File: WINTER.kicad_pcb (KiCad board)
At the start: 6 copper layers, 52 x 34 mm, 107 parts, among them J1 Amphenol ICC 10118193-0001LF, J2 TF-102-15, J3 Screw_Terminal_01x12, J4 Screw_Terminal_01x02, J5 Conn_01x05, J6 Conn_01x04, Q1 SI7232DN-T1-GE3, Q2 SI7232DN-T1-GE3, Q3 SI7232DN-T1-GE3, SW1 A6S-2104-H, U1 LM2940LD-5.0/NOPB, U10 SX1262IMLTRT, U11 MAX-M10S-00B, U12 LM1117LD-3.3/NOPB, U13 74LVC1G04, U15 TPS7A20xxxDQN, U2 DRV8210DRLR, U3 MMC5983MA, U4 ICM-42688-P, U5 SKY66105, U6 STM32H725RGV6, U7 MS5607-02BA, U8 ADXL375, U9 SN74LVC2T45DC, Y1 ECS-2520MV-240-BN, Y2 ATX-11-F-32.000MHZ-F05-T

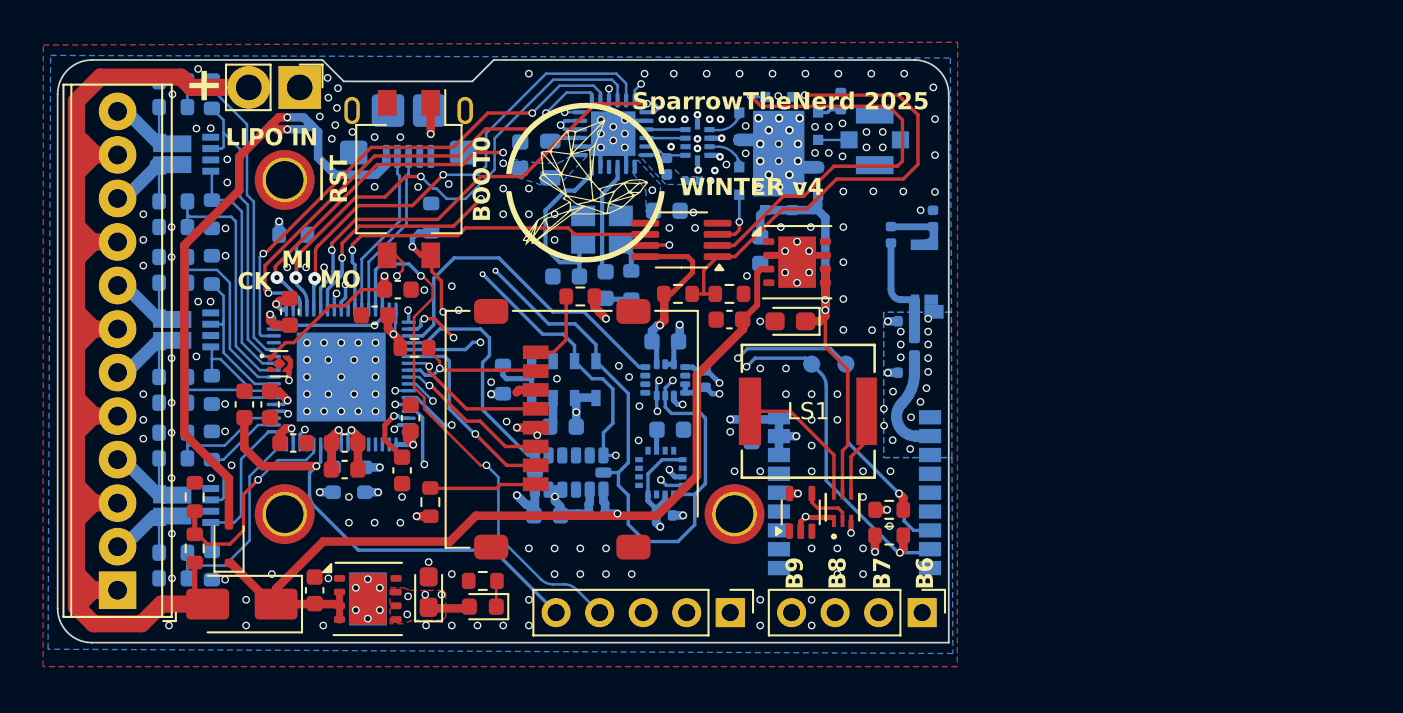
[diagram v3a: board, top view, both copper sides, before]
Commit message: Started new layout and updated power circuitry
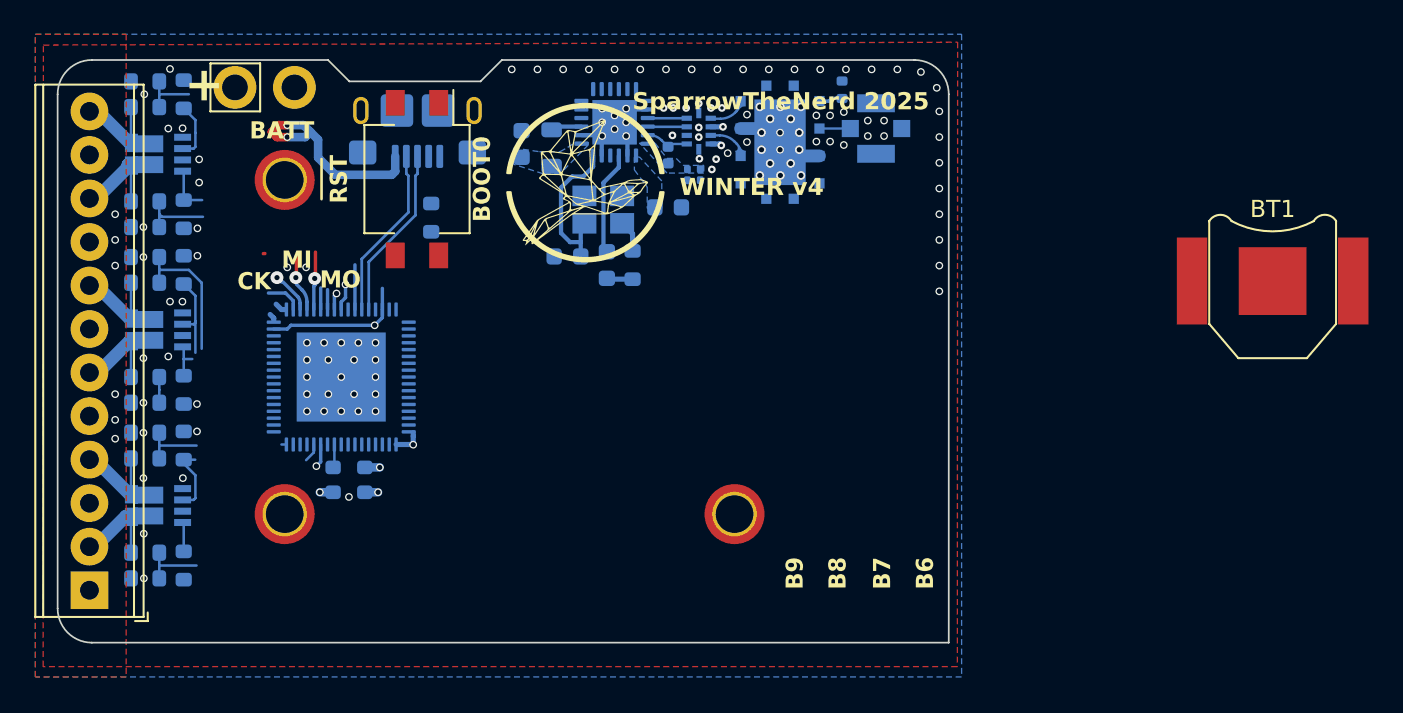
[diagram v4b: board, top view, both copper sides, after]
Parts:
- removed AE2: GGBLA.01.A, WINTERfootprints:GGBLA.01.A
- removed C1, C3: 2.2uF, Capacitor_SMD:C_0603_1608Metric
- removed C10: 4.7uF, Capacitor_SMD:C_0603_1608Metric
- removed C11: 470nF, Capacitor_SMD:C_0603_1608Metric
- removed C12: 22uF, Capacitor_SMD:C_0603_1608Metric
- removed C13, C14: 47uF tant, Capacitor_Tantalum_SMD:CP_EIA-2012-15_AVX-P
- removed C15, C19: 1uF, Capacitor_SMD:C_0402_1005Metric
- removed C16, C2, C20, C21, C26, C29, C4, C5, C6, C7, C8, C9: 100nF, Capacitor_SMD:C_0603_1608Metric
- removed C17: 10uF, Capacitor_SMD:C_0603_1608Metric
- removed C18: 2.2uF, Capacitor_SMD:C_0402_1005Metric
- removed C30: 0.8pF, Capacitor_SMD:C_0402_1005Metric
- removed C31: 2.7pF, Capacitor_SMD:C_0402_1005Metric
- removed C32: 0.5pF, Capacitor_SMD:C_0402_1005Metric
- removed C33: 22pF, Capacitor_SMD:C_0402_1005Metric
- removed C34: DNP, Capacitor_SMD:C_0402_1005Metric
- removed D1: RSX501L-20TE25, Diode_SMD:D_SMA
- removed D2: PMEG3020EJ, Diode_SMD:D_SOD-323F
- removed D3: LED_RD, LED_SMD:LED_0603_1608Metric
- removed J2: TF-102-15, Connector_Card:microSD_HC_Molex_47219-2001
- removed J5: Conn_01x05, Connector_PinHeader_2.54mm:PinHeader_1x05_P2.54mm_Vertical
- removed J6: Conn_01x04, Connector_PinHeader_2.54mm:PinHeader_1x04_P2.54mm_Vertical
- removed LS1: AST0760MCTRQ, WINTERfootprints:AST0760_MAL
- removed R22, R23, R5, R6: 10k, Resistor_SMD:R_0603_1608Metric
- removed R24, R30: 27k, Resistor_SMD:R_0603_1608Metric
- removed R28, R29, R3, R4: 4.7k, Resistor_SMD:R_0603_1608Metric
- removed R31: 100k, Resistor_SMD:R_0603_1608Metric
- removed R7: 470, Resistor_SMD:R_0603_1608Metric
- removed TP1, TP2: TestPoint, TestPoint:TestPoint_Pad_D1.0mm
- removed U1: LM2940LD-5.0/NOPB, Package_SON:WSON-8-1EP_4x4mm_P0.8mm_EP2.2x3mm
- removed U11: MAX-M10S-00B, WINTERfootprints:MAX-M10S-00B
- removed U12: LM1117LD-3.3/NOPB, Package_SON:WSON-8-1EP_4x4mm_P0.8mm_EP2.2x3mm
- removed U13: 74LVC1G04, Package_TO_SOT_SMD:Texas_R-PDSO-G5_DCK-5
- removed U15: TPS7A20xxxDQN, Package_SON:Texas_X2SON-4_1x1mm_P0.65mm
- removed U2: DRV8210DRLR, WINTERfootprints:SOT_210DRLR_TEX
- removed U3: MMC5983MA, WINTERfootprints:MMC5983MA_MEM
- removed U4: ICM-42688-P, WINTERfootprints:PQFN50P300X250X97-14N
- removed U7: MS5607-02BA, Package_LGA:LGA-8_3x5mm_P1.25mm
- removed U8: ADXL375, Package_LGA:LGA-14_3x5mm_P0.8mm_LayoutBorder1x6y
- removed U9: SN74LVC2T45DC, Package_SO:MSOP-8_3x3mm_P0.65mm
- added BT1: 2998TR, Battery:BatteryHolder_Keystone_2998_1x6.8mm, F.Cu at (208.9, 96.9)
- moved J3 1.64 mm to (139.9, 114.9)
- moved Q1 1.64 mm to (143.9, 110.0)
- moved Q2 1.64 mm to (143.9, 99.8)
- moved Q3 1.64 mm to (143.9, 89.5)
- moved R10 1.64 mm to (143.1, 104.0)
- moved R11 1.64 mm to (143.1, 95.5)
- moved R14 1.64 mm to (145.4, 113.5)
- moved R15 1.64 mm to (145.4, 106.5)
- moved R16 1.64 mm to (145.4, 103.2)
- moved R17 1.64 mm to (145.4, 96.2)
- moved R18 1.64 mm to (145.4, 93.0)
- moved R19 1.64 mm to (145.4, 86.0)
- moved R20 1.64 mm to (143.1, 114.2)
- moved R32 1.64 mm to (143.1, 107.2)
- moved R33 1.64 mm to (143.1, 93.8)
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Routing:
- net LIPO+: track 79.8 -> 0.00 mm, vias 0 -> 1
- net SCL: track 73.0 -> 1.57 mm, vias 5 -> 1
- net +3V3: track 67.1 -> 3.98 mm, vias 39 -> 3
- net SDA: track 62.1 -> 0.99 mm, vias 8 -> 1
- net Net-(D1-K): track 51.1 -> 0.00 mm
- net SWD-NRST: track 48.0 -> 1.37 mm, vias 2 -> 1
- net SWCLK: track 40.6 -> 0.00 mm, vias 1 -> 0
- net SERVO4: track 37.0 -> 0.00 mm, vias 1 -> 0
- net SERVO3: track 35.0 -> 0.00 mm, vias 1 -> 0
- net BUZZ: track 33.8 -> 0.00 mm, vias 3 -> 0
- net SERVO2: track 33.2 -> 0.00 mm, vias 1 -> 0
- net SCK_LoRa: track 33.8 -> 2.47 mm, vias 3 -> 1
- net SWDIO: track 31.3 -> 0.00 mm, vias 2 -> 0
- net LoRa_BUSY: track 29.7 -> 0.10 mm, vias 2 -> 0
- net SERVO1: track 29.4 -> 0.00 mm, vias 1 -> 0
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- added copper zone on F.Cu, net LIPO+
- added copper zone on In2.Cu, net LIPO+
- added copper zone on In3.Cu, net LIPO+
- removed copper zone on F.Cu, net +3V3
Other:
- outline, holes or cut-outs redrawn
- board text added: "BATT"
- board text removed: "LIPO IN"

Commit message: updated power delivery and component choices. v4 now ready
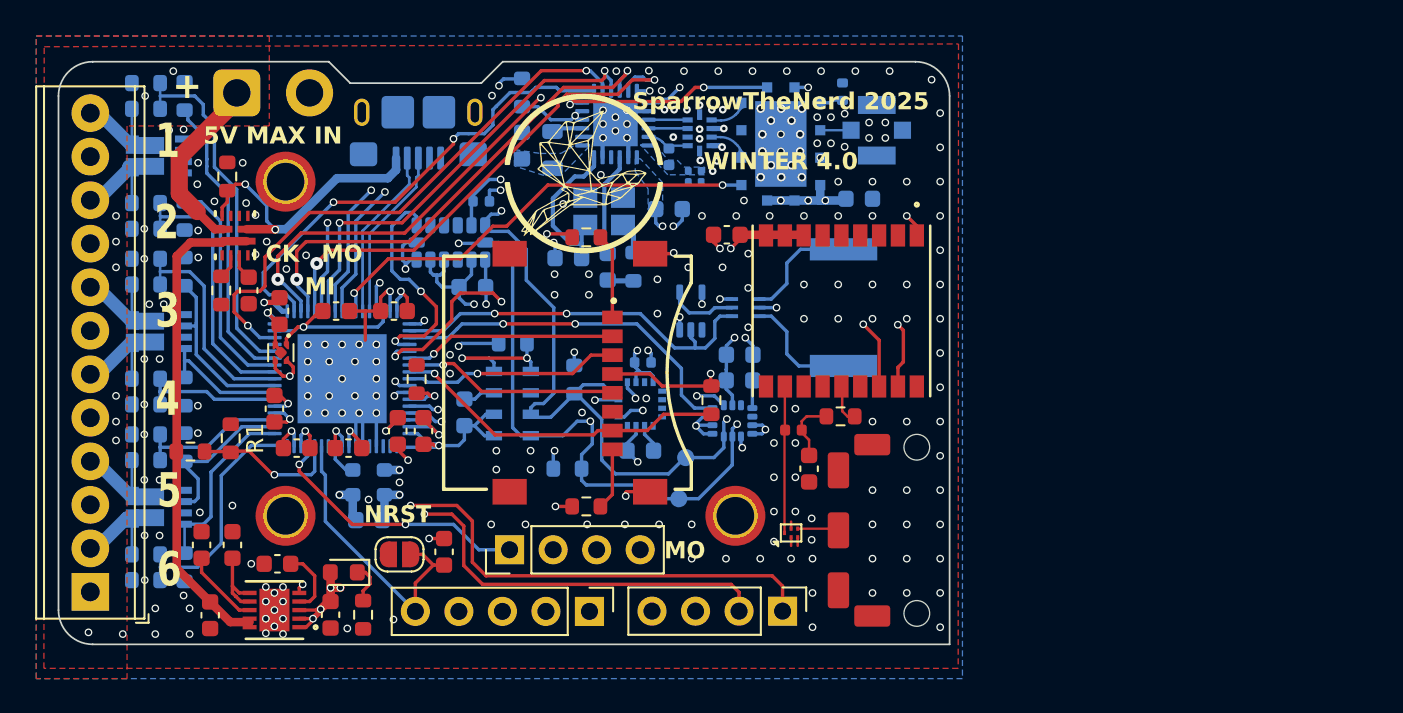
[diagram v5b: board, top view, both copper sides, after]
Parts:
- removed BT1: 2998TR, Battery:BatteryHolder_Keystone_2998_1x6.8mm
- removed SW1: A6S-2104-H, Button_Switch_SMD:SW_DIP_SPSTx02_Slide_Omron_A6S-210x_W8.9mm_P2.54mm
- added AE2: AP.10H.01, WINTERfootprints:AP.10H.01, F.Cu at (183.6, 111.4)
- added C1: 2.2uF, Capacitor_SMD:C_0603_1608Metric, F.Cu at (154.2, 98.7)
- added C10: 4.7uF, Capacitor_SMD:C_0603_1608Metric, B.Cu at (156.2, 110.8)
- added C11: 22uF, Capacitor_SMD:C_0603_1608Metric, F.Cu at (153.9, 116.4)
- added C12: 22uF, Capacitor_SMD:C_0603_1608Metric, F.Cu at (146.9, 116.4)
- added C13: 10nF, Capacitor_SMD:C_0603_1608Metric, F.Cu at (181.8, 107.8)
- added C14: 100nF, Capacitor_SMD:C_0603_1608Metric, F.Cu at (149.2, 97.5)
- added C15: 1uF, Capacitor_SMD:C_0402_1005Metric, B.Cu at (172.2, 101.7)
- added C16: 100nF, Capacitor_SMD:C_0603_1608Metric, B.Cu at (177.8, 102.7)
- added C17: 10nF, Capacitor_SMD:C_0603_1608Metric, B.Cu at (172.0, 106.8)
- added C18: 2.2uF, Capacitor_SMD:C_0603_1608Metric, B.Cu at (177.8, 101.2)
- added C19: 1uF, Capacitor_SMD:C_0402_1005Metric, B.Cu at (162.7, 92.2)
- added C2: 100nF, Capacitor_SMD:C_0603_1608Metric, F.Cu at (160.6, 112.7)
- added C20: 100nF, Capacitor_SMD:C_0603_1608Metric, B.Cu at (162.2, 97.2)
- added C21: 100nF, Capacitor_SMD:C_0603_1608Metric, B.Cu at (161.7, 104.6)
- added C26: 100nF, Capacitor_SMD:C_0603_1608Metric, B.Cu at (184.8, 92.1)
- added C29: 100nF, Capacitor_SMD:C_0603_1608Metric, F.Cu at (177.1, 94.2)
- added C3: 2.2uF, Capacitor_SMD:C_0603_1608Metric, F.Cu at (157.8, 105.7)
- added C30: 22uF, Capacitor_SMD:C_0603_1608Metric, F.Cu at (146.4, 112.3)
- added C31: 22uF, Capacitor_SMD:C_0603_1608Metric, F.Cu at (148.2, 112.3)
- added C32: 22uF, Capacitor_SMD:C_0603_1608Metric, F.Cu at (150.8, 113.4)
- added C4: 100nF, Capacitor_SMD:C_0603_1608Metric, F.Cu at (150.7, 104.3)
- added C5: 100nF, Capacitor_SMD:C_0603_1608Metric, F.Cu at (155.0, 106.7)
- added C6: 100nF, Capacitor_SMD:C_0603_1608Metric, F.Cu at (151.9, 106.7)
- added C7: 100nF, Capacitor_SMD:C_0603_1608Metric, F.Cu at (150.9, 98.7)
- added C8: 100nF, Capacitor_SMD:C_0603_1608Metric, F.Cu at (159.3, 105.7)
- added C9: 100nF, Capacitor_SMD:C_0603_1608Metric, F.Cu at (157.6, 98.7)
- added D3: LED_RD, LED_SMD:LED_0603_1608Metric, F.Cu at (154.7, 113.9)
- added FL2: B39162B8813P810, Filter:Filter_1109-5_1.1x0.9mm, F.Cu at (180.8, 111.6)
- added J2: TF-102-15, WINTERfootprints:microSD_GCT_MEM2067-02-180-00, F.Cu at (167.8, 102.2)
- added J5: Conn_01x05, Connector_PinHeader_2.54mm:PinHeader_1x05_P2.54mm_Vertical, F.Cu at (169.0, 116.2)
- added J6: Conn_01x04, Connector_PinHeader_2.54mm:PinHeader_1x04_P2.54mm_Vertical, F.Cu at (180.3, 116.2)
- added J7: Conn_01x04, Connector_PinHeader_2.54mm:PinHeader_1x04_P2.54mm_Vertical, F.Cu at (164.4, 112.6)
- added JP1: SolderJumper_2_Open, Jumper:SolderJumper-2_P1.3mm_Open_RoundedPad1.0x1.5mm, F.Cu at (157.9, 112.8)
- added L3: 27nH, Inductor_SMD:L_0402_1005Metric, F.Cu at (180.9, 105.6)
- added LS1: AST0760MCTRQ, WINTERfootprints:AST0760_MAL, B.Cu at (183.9, 98.5)
- added R1: 27k, Resistor_SMD:R_0603_1608Metric, F.Cu at (148.1, 106.1)
- added R12: 27k, Resistor_SMD:R_0603_1608Metric, F.Cu at (147.9, 90.8)
- added R13: 27k, Resistor_SMD:R_0603_1608Metric, F.Cu at (147.6, 97.5)
- added R21: 10, 0.25W, Resistor_SMD:R_0603_1608Metric, F.Cu at (183.7, 104.8)
- added R22: 10k, Resistor_SMD:R_0603_1608Metric, B.Cu at (164.6, 100.5)
- added R28: 4.7k, Resistor_SMD:R_0603_1608Metric, F.Cu at (168.8, 110.0)
- added R29: 4.7k, Resistor_SMD:R_0603_1608Metric, F.Cu at (168.8, 94.3)
- added R3: 4.7k, Resistor_SMD:R_0603_1608Metric, F.Cu at (176.2, 103.8)
- added R30: 27k, Resistor_SMD:R_0603_1608Metric, F.Cu at (145.8, 106.8)
- added R4: 4.7k, Resistor_SMD:R_0603_1608Metric, B.Cu at (165.1, 85.9)
- added R5: 4.7k, Resistor_SMD:R_0603_1608Metric, B.Cu at (168.2, 102.7)
- added R6: 4.7k, Resistor_SMD:R_0603_1608Metric, B.Cu at (167.8, 107.8)
- added R7: 470, Resistor_SMD:R_0603_1608Metric, F.Cu at (155.8, 116.4)
- added TP1: TestPoint, TestPoint:TestPoint_Pad_D1.0mm, B.Cu at (174.7, 107.2)
- added TP2: TestPoint, TestPoint:TestPoint_Pad_D1.0mm, B.Cu at (174.2, 109.6)
- added U1: ADP7158ACPZ-3.3-R7, WINTERfootprints:CP-10-9_ADI, F.Cu at (150.7, 116.1)
- added U11: MAX-M10S-00B, WINTERfootprints:MAX-M10S-00B, F.Cu at (183.7, 98.6)
- added U12: TPS2121RUXR, WINTERfootprints:RUX0012A, F.Cu at (148.3, 94.2)
- added U13: 74LVC1G04, Package_TO_SOT_SMD:Texas_R-PDSO-G5_DCK-5, B.Cu at (174.9, 98.7)
- added U15: TPS7A20135PDQNR, Package_SON:Texas_X2SON-4_1x1mm_P0.65mm, F.Cu at (151.0, 101.1)
- added U2: DRV8210DRLR, WINTERfootprints:SOT_210DRLR_TEX, B.Cu at (178.2, 98.5)
- added U3: MMC5983MA, WINTERfootprints:MMC5983MA_MEM, B.Cu at (172.0, 104.1)
- added U4: ICM-42688-P, WINTERfootprints:PQFN50P300X250X97-14N, B.Cu at (177.4, 105.1)
- added U7: MS5607-02BA, Package_LGA:LGA-8_3x5mm_P1.25mm, B.Cu at (164.5, 104.0)
- added U8: ADXL375, Package_LGA:LGA-14_3x5mm_P0.8mm_LayoutBorder1x6y, B.Cu at (160.9, 94.7)
- J4: footprint Connector_PinHeader_2.54mm:PinHeader_1x02_P2.54mm_Vertical -> Connector_Wire:SolderWire-0.75sqmm_1x02_P7mm_D1.25mm_OD3.5mm
- R10, R11, R20, R33, R34, R9: value 100k -> 27k
- R2: moved to F.Cu
- moved R2 9.46 mm to (158.9, 102.6)
- moved J4 2.88 mm to (148.5, 85.9), turned to 0 degrees
- moved Y1 1.16 mm to (156.1, 108.6)
- moved R25 0.12 mm to (183.8, 85.8)
- moved C23 0.11 mm to (173.7, 92.7)
- moved C24 0.11 mm to (175.6, 90.8)
- moved J3 0.11 mm to (139.9, 115.0)
- moved C25 0.11 mm to (174.8, 90.8)
- moved C28 0.11 mm to (167.8, 95.6)
- moved FL1 0.11 mm to (175.5, 88.2)
- moved H1 0.11 mm to (151.3, 91.1)
- moved H2 0.11 mm to (177.6, 110.6)
- moved H3 0.11 mm to (151.3, 110.6)
- moved J1 0.11 mm to (159.1, 87.0)
- moved L2 0.11 mm to (173.7, 89.7)
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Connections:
- net /Microcontroller/SWD-BOOT0 renamed Net-(U6-BOOT0)
- J1 pad 1: Net-(D2-A) -> /Power/VBUS
- J4 pad 1: GNDREF -> LIPO+
- J4 pad 2: LIPO+ -> GNDREF
- U5 pad 1: /LoRa Radio/PA-EN-2v5 -> LoRa_PA-EN
- U5 pad 10: +5V -> +3V3
- U5 pad 11: +5V -> +3V3
- U5 pad 12: +5V -> +3V3
- U5 pad 5: /LoRa Radio/DIO2-2v5 -> /LoRa Radio/DIO2
- U5 pad 6: +2V5 -> +3V3
- U6 pad 12: SWD-NRST -> NRST
- U6 pad 14: unconnected-(U6-PC1-Pad14) -> CS_EXT
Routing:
- net +3V3: track 3.98 -> 89.5 mm, vias 3 -> 37
- net SCL: track 1.57 -> 68.6 mm, vias 1 -> 6
- net SDA: track 0.99 -> 67.1 mm, vias 1 -> 4
- net MISO_LoRa: track 3.31 -> 68.1 mm, vias 1 -> 3
- net GNDREF: track 10.3 -> 74.2 mm, vias 127 -> 257
- net SCK_LoRa: track 2.47 -> 60.4 mm, vias 1 -> 3
- net MOSI_LoRa: track 3.39 -> 58.9 mm, vias 1 -> 2
- net SERVO4: track 0.00 -> 36.9 mm, vias 0 -> 2
- net SERVO3: track 0.00 -> 34.8 mm, vias 0 -> 2
- net CS_LoRa: track 1.26 -> 34.9 mm, vias 0 -> 2
- net LoRa_BUSY: track 0.10 -> 32.6 mm, vias 0 -> 2
- net /Power/VOut: track 0.00 -> 28.2 mm
- net SERVO2: track 0.00 -> 26.4 mm, vias 0 -> 1
- net LoRa_INT: track 2.15 -> 28.2 mm, vias 0 -> 2
- net LoRa_RST: track 1.16 -> 26.1 mm, vias 0 -> 2
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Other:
- board text added: "5V MAX IN"
- board text added: "B6 B7 B8 B9"
- board text added: "NRST"
- board text added: "V G C D R"
- board text added: "WINTER 4.0"
- board text removed: "3V3"
- board text removed: "B6"
- board text removed: "B7"
- board text removed: "B8"
- board text removed: "B9"
- board text removed: "BATT"
- board text removed: "BOOT0"
- board text removed: "GND"
- board text removed: "RST"
- board text removed: "SWC"
- board text removed: "SWD"
- board text removed: "WINTER v4"

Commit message: Fixed power distribution and made small improvements. Updated revision number
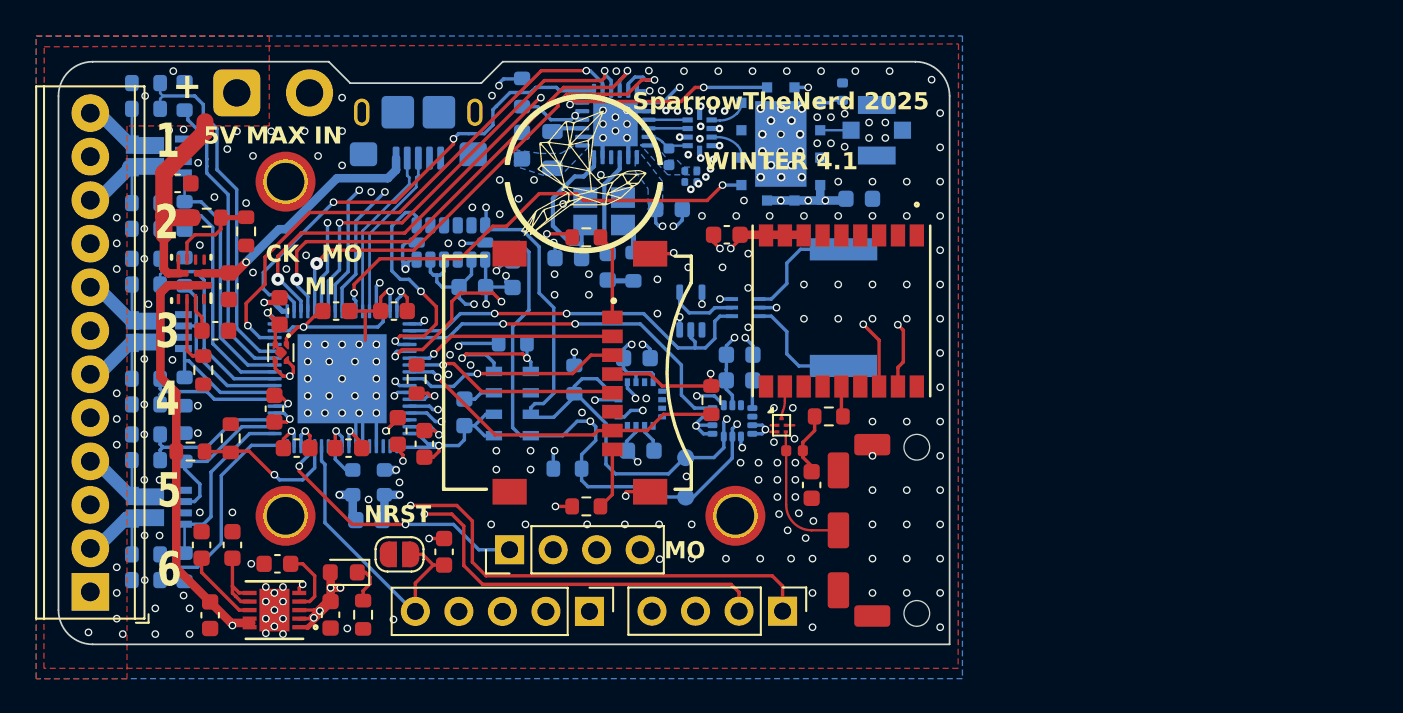
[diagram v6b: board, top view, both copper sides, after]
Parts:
- removed C19: 1uF, Capacitor_SMD:C_0402_1005Metric
- removed U12: TPS2121RUXR, WINTERfootprints:RUX0012A
- added C33: 22uF, Capacitor_SMD:C_0603_1608Metric, F.Cu at (145.0, 91.2)
- added C34: 22uF, Capacitor_SMD:C_0603_1608Metric, F.Cu at (148.0, 97.2)
- added C35: 1uF, Capacitor_SMD:C_0603_1608Metric, B.Cu at (164.6, 96.5)
- added R23: 374k, Resistor_SMD:R_0603_1608Metric, F.Cu at (149.0, 94.0)
- added U9: SN74LVC1G04DCKR, WINTERfootprints:RUX0012A, F.Cu at (145.8, 96.8)
- C14: value 100nF -> 1uF
- C15: footprint Capacitor_SMD:C_0402_1005Metric -> Capacitor_SMD:C_0603_1608Metric
- C30, C31, C32: value 22uF -> 1uF
- FL1: value 0900FM15D0039E -> 0900FM15K0039001E
- R12: value 27k -> 100k
- moved FL2 6.31 mm to (180.2, 105.3), turned to -90 degrees
- moved R13 4.77 mm to (146.5, 102.1)
- moved C14 3.05 mm to (147.2, 99.8), turned to 0 degrees
- moved R12 2.68 mm to (146.7, 93.2), turned to 180 degrees
- moved L3 1.21 mm to (181.0, 106.8)
- moved C13 0.96 mm to (182.0, 108.8)
- moved C8 0.75 mm to (159.4, 106.4)
- moved R21 0.69 mm to (183.0, 104.8)
- moved C15 0.43 mm to (171.8, 101.4)
- moved TP2 0.39 mm to (174.6, 109.5)
- moved C24 0.25 mm to (175.3, 90.8)
- moved C25 0.20 mm to (174.6, 90.8)
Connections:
- C12 pad 2: /Power/VOut -> /Power/VMux
- L3 pad 1: /GPS/GPS_RFIN -> /GPS/GPS_ANT
- R12 pad 1: /Power/VBUS -> Net-(U9-OV1)
- R12 pad 2: GNDREF -> LIPO+
- R30 pad 2: /Power/VOut -> /Power/VMux
- U1 pad 10: /Power/VOut -> /Power/VMux
- U1 pad 5: +3V3 -> /Power/VMux
- U1 pad 9: /Power/VOut -> /Power/VMux
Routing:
- net /Power/VMux: track 0.00 -> 31.8 mm, vias 0 -> 2
- net /Power/VOut: track 28.2 -> 0.00 mm
- net /GPS/GPS_RFIN: track 8.63 -> 1.98 mm
- net GNDREF: track 74.2 -> 68.4 mm, vias 257 -> 285
- net /GPS/GPS_ANT: track 2.50 -> 8.19 mm
- net Net-(U9-OV1): track 0.00 -> 5.46 mm
- net LIPO+: track 10.7 -> 13.6 mm
- net Net-(U9-ILM): track 1.45 -> 4.08 mm
- net /Power/VBUS: track 17.0 -> 14.5 mm, vias 2 -> 1
- net +3V3: track 89.5 -> 91.8 mm, vias 37 -> 36
- net SCL: track 68.6 -> 70.0 mm
- net LoRa_BUSY: track 32.6 -> 31.3 mm
- net LoRa_PA-EN: track 26.3 -> 26.9 mm
- net SDA: track 67.1 -> 67.7 mm
- net Net-(U9-SS): track 1.50 -> 2.01 mm
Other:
- board text added: "V G CK DT R"
- board text added: "WINTER 4.1"
- board text removed: "V G C D R"
- board text removed: "WINTER 4.0"
